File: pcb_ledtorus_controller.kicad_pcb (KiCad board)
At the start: 2 copper layers, 81 parts, among them J1 CONN_01X04, P1 CONN_4X2, P2 CONN_9, P5 CONN_3X2, P6 CONN_3, U1 TM4C1232XXPM, U3 KNUSB, U4 L6234, U5 LP2985LV, U6 TS3001x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

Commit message: Starting on netlist
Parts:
- added P3: CONN_01X09, knielsenlib:DualShock_conn, F.Cu at (76.0, 147.0)
- added P4: CONN_01X09, knielsenlib:DualShock_conn, F.Cu at (124.0, 147.0)
- added SW1: Switch_3, knielsenlib:DIPSWITCH_X3, F.Cu at (68.0, 69.0)
- J1: footprint Pin_Headers:Pin_Header_Straight_1x04_Pitch1.27mm -> Pin_Headers:Pin_Header_Straight_1x04_Pitch2.54mm
- P1: footprint Pin_Headers:Pin_Header_Straight_2x04_Pitch1.27mm -> Pin_Headers:Pin_Header_Straight_2x04_Pitch2.54mm
- P2: footprint Pin_Headers:Pin_Header_Straight_1x09_Pitch1.27mm -> Pin_Headers:Pin_Header_Straight_1x09_Pitch2.54mm
- P5: footprint Pin_Headers:Pin_Header_Straight_2x03_Pitch1.27mm -> Pin_Headers:Pin_Header_Straight_2x03_Pitch2.54mm
- moved C11 173.0 mm to (89.6, 109.4)
- moved C13 173.0 mm to (99.6, 95.1)
- moved C2 173.0 mm to (93.7, 89.8)
- moved C5 173.0 mm to (94.0, 110.5)
- moved C6 173.0 mm to (89.6, 114.4)
- moved C8 173.0 mm to (99.6, 89.8)
- moved P1 173.0 mm to (92.8, 95.0)
- moved B1 173.0 mm to (75.8, 94.8)
- moved C1 173.0 mm to (92.7, 104.1)
- moved C10 173.0 mm to (96.9, 105.4)
- moved C12 173.0 mm to (88.8, 104.1)
- moved C3 173.0 mm to (99.8, 100.4)
- moved C4 173.0 mm to (101.2, 105.4)
- moved C7 173.0 mm to (85.5, 109.4)
- moved C9 173.0 mm to (81.6, 111.6)
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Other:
- board outline added: 100 x 100 mm

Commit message: Work on layout
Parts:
- removed D8, D9: LED, LEDs:LED_0805
- removed R28, R29: 1k, Resistors_SMD:R_0805
- added H1: mounting_hole, Mounting_Holes:MountingHole_4.3mm_M4, F.Cu at (55.0, 87.0)
- added H2: mounting_hole, Mounting_Holes:MountingHole_4.3mm_M4, F.Cu at (145.0, 87.0)
- added H3: mounting_hole, Mounting_Holes:MountingHole_4.3mm_M4, F.Cu at (55.0, 142.0)
- added H4: mounting_hole, Mounting_Holes:MountingHole_4.3mm_M4, F.Cu at (145.0, 142.0)
- C15: footprint Capacitors_SMD:C_0603 -> w_smd_cap:c_elec_6.3x5.3
- D3, D5, D6, D7: footprint Diodes_SMD:D_SOD-123F -> Diodes_SMD:D_SOD-123
- P6: footprint knielsenlib:con-jack-DCJ0303 -> w_conn_misc:dc_socket
- R12, R13, R14: footprint Resistors_SMD:R_0612 -> Resistors_SMD:R_0603
- moved U3 98.0 mm to (51.5, 132.0)
- moved R22 72.6 mm to (99.9, 113.3)
- moved R30 65.7 mm to (119.7, 143.5), turned to 270 degrees
- moved R13 64.6 mm to (103.3, 118.3)
- moved R18 64.1 mm to (103.3, 120.8)
- moved R21 64.0 mm to (103.2, 113.3)
- moved R6 63.8 mm to (110.8, 115.8)
- moved D3 63.1 mm to (107.0, 115.8), turned to 180 degrees
- moved C15 60.2 mm to (107.0, 106.0), turned to 315 degrees
- moved R8 60.0 mm to (99.9, 115.8), turned to 180 degrees
- moved D5 54.7 mm to (107.0, 118.3), turned to 180 degrees
- moved SW1 54.3 mm to (56.0, 122.0), turned to 270 degrees
- moved D1 53.9 mm to (106.0, 135.5), turned to 90 degrees
- moved R19 53.9 mm to (99.9, 120.8)
- moved R14 53.8 mm to (99.9, 118.3)
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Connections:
- net Net-(C19-Pad2) renamed /Power/vsw
- net Net-(R31-Pad2) renamed /Power/fb
- P5 pad 1: +24V -> usb5v
- P5 pad 3: +8V -> +24V
- P5 pad 5: usb5v -> +8V
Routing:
- net /Motor/phase_c: track 0.00 -> 57.5 mm, vias 0 -> 4
- net /Motor/phase_a: track 0.00 -> 46.4 mm, vias 0 -> 4
- net /Motor/phase_b: track 0.00 -> 44.7 mm, vias 0 -> 4
- net +24V: track 0.00 -> 34.8 mm, vias 0 -> 3
- net /Motor/neutral: track 0.00 -> 32.3 mm, vias 0 -> 1
- net +8V: track 0.00 -> 29.5 mm
- net GND: track 0.00 -> 19.1 mm, vias 0 -> 12
- net VCC: track 0.00 -> 11.6 mm
- net /Power/vsw: track 0.00 -> 11.1 mm
- net /Power/fb: track 0.00 -> 6.75 mm
- net Net-(C19-Pad1): track 0.00 -> 3.71 mm
- net /Motor/m_sense1_raw: track 0.00 -> 2.70 mm
- net +3V3: track 0.00 -> 2.63 mm
- net /Power/bypass: track 0.00 -> 2.42 mm
- added copper zone on F.Cu, net +24V
- added copper zone on F.Cu, net +8V
- added copper zone on F.Cu, net GND
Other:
- board size 100 x 100 mm -> 100 x 68 mm
- copper layers 2 -> 4
- net class Default: clearance 0.2 -> 0; trace_width 0.25 -> 0.2032; via_dia 0.8 -> 0.635; via_drill 0.4 -> 0.3
- net class Tight added: clearance 0.1524, trace_width 0.1524, via_dia 0.635, via_drill 0.3
- rule trace_clearance: 0.2 -> 0
- rule trace_min: 0.2 -> 0.1524
- rule via_min_size: 0.4 -> 0.635

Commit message: Initial routing complete
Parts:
- moved R25 40.0 mm to (64.1, 142.9), turned to 270 degrees
- moved D2 28.8 mm to (100.3, 143.0)
- moved R5 28.8 mm to (100.3, 145.5)
- moved R22 5.73 mm to (100.5, 119.0), turned to 90 degrees
- moved D7 5.00 mm to (107.0, 118.3)
- moved R20 5.00 mm to (110.8, 118.3)
- moved R21 5.00 mm to (103.2, 118.3)
- moved R19 4.74 mm to (104.1, 123.0), turned to 180 degrees
- moved B1 3.90 mm to (66.5, 129.6)
- moved R27 3.71 mm to (95.9, 145.6), turned to 180 degrees
- moved R26 3.30 mm to (73.9, 144.7), turned to 0 degrees
- moved D3 2.50 mm to (107.0, 113.3)
- moved D5 2.50 mm to (107.0, 115.8)
- moved R12 2.50 mm to (110.8, 115.8)
- moved R13 2.50 mm to (103.3, 115.8)
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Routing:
- net usb5v: track 0.00 -> 111.7 mm, vias 0 -> 1
- net ps2_clk: track 0.00 -> 92.5 mm, vias 0 -> 1
- net m_en2: track 0.00 -> 90.8 mm, vias 0 -> 2
- net ps2_ack: track 0.00 -> 89.1 mm, vias 0 -> 1
- net ps2_data: track 0.00 -> 80.4 mm, vias 0 -> 1
- net /reset: track 0.00 -> 78.8 mm, vias 0 -> 2
- net ps2_cmd: track 0.00 -> 75.1 mm, vias 0 -> 1
- net m_en1: track 0.00 -> 74.6 mm, vias 0 -> 2
- net m_in2: track 0.00 -> 73.4 mm, vias 0 -> 2
- net m_in1: track 0.00 -> 72.1 mm, vias 0 -> 2
- net +8V: track 29.5 -> 94.3 mm
- net m_sense1: track 0.00 -> 64.1 mm, vias 0 -> 2
- net /u0rx: track 0.00 -> 54.5 mm
- net /tdi: track 0.00 -> 54.2 mm, vias 0 -> 2
- net /u0tx: track 0.00 -> 52.9 mm
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- added copper zone on In2.Cu, net +24V
- added copper zone on In2.Cu, net +3V3
- added copper zone on B.Cu, net GND
- added copper zone on In1.Cu, net GND
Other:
- net class Default: clearance 0 -> 0.2
- rule trace_clearance: 0 -> 0.2

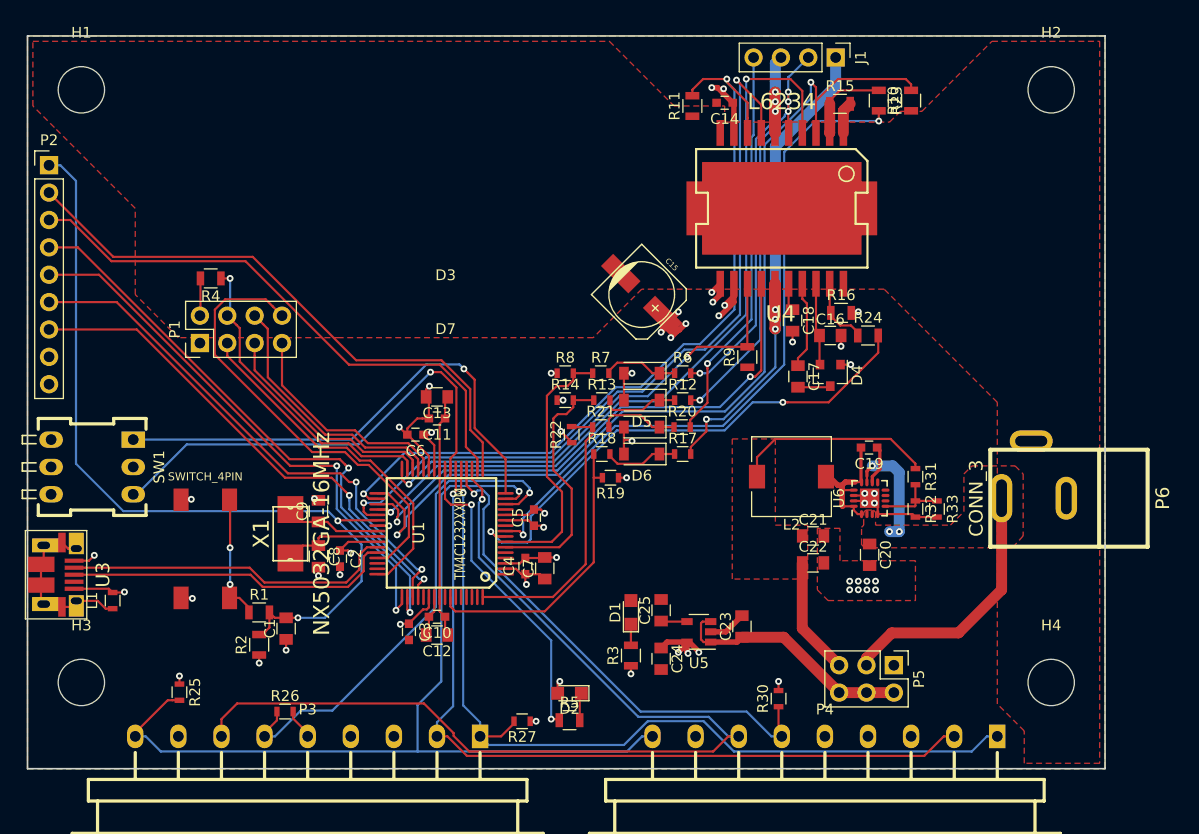
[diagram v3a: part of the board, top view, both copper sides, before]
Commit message: Completing cleanups and ToDos:
 - L6234 thermal vias done
 - Gerbers checked
 - Misc. io and stuff tweaks
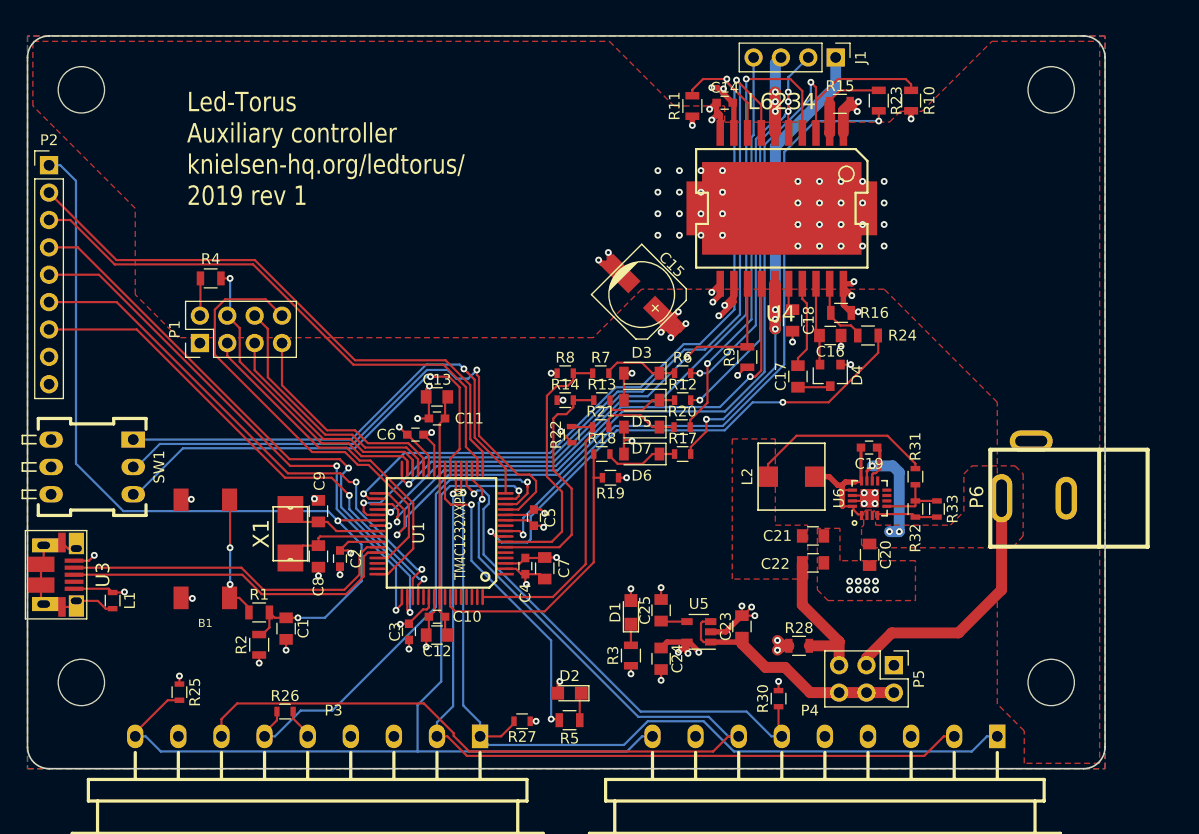
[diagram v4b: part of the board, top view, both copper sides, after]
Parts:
- added R28: 0, Resistors_SMD:R_0805, F.Cu at (121.6, 138.6)
- L2: footprint Inductors_SMD:L_7.3x7.3_H3.5 -> knielsenlib:Coil_WE_7447786004
- P6: footprint w_conn_misc:dc_socket -> knielsenlib:dc_socket
- U4: footprint knielsenlib:POWERSO20 -> knielsenlib:POWERSO20_stencil
- U6: footprint Housings_DFN_QFN:QFN-16-1EP_3x3mm_Pitch0.5mm -> knielsenlib:QFN16-TS30001
- turned L2 to 270 degrees
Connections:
- P3 pad 3: +8V -> /PS2_Controllers/rumble
- P4 pad 3: +8V -> /PS2_Controllers/rumble
- SW1 pad 1: gpio2 -> gpio3
- SW1 pad 3: Net-(SW1-Pad3) -> gpio2
- U1 pad 13: Net-(U1-Pad13) -> gpio2
- U1 pad 16: gpio2 -> gpio3
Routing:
- net /PS2_Controllers/rumble: track 0.00 -> 70.6 mm, vias 0 -> 2
- net +8V: track 94.3 -> 31.3 mm
- net gpio3: track 0.00 -> 46.9 mm, vias 0 -> 1
- net GND: track 71.0 -> 96.4 mm, vias 36 -> 92
- net gpio2: track 46.9 -> 54.0 mm
- net /Power/vsw: track 12.3 -> 13.3 mm
- net /usb_dm: track 30.9 -> 31.7 mm
- net /usb_dp: track 30.7 -> 31.6 mm
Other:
- outline, holes or cut-outs redrawn
- net class Default: clearance 0.2 -> 0
- rule trace_clearance: 0.2 -> 0
- board text added: "Led-Torus Auxiliary controller knielsen-hq.org/ledtorus/ 2019 rev 1"

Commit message: Submitted rev1 for production @ SeeedStudio
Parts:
- C15: footprint w_smd_cap:c_elec_6.3x5.3 -> w_smd_cap:c_elec_6.3x7.7
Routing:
- net +24V: track 56.9 -> 60.3 mm
- net +8V: track 31.3 -> 32.2 mm
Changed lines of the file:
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@@
     (thickness 1.6)
     (drawings 13)
-    (tracks 1038)
+    (tracks 1040)
     (zones 0)
     (modules 85)
@@
   )
   (setup
-    (last_trace_width 0.2032)
+    (last_trace_width 0.508)
     (user_trace_width 0.1524)
     (user_trace_width 0.2032)
@@
       (drillshape 0)
       (scaleselection 1)
-      (outputdirectory gerbers))
+      (outputdirectory gerbers_rev1))
   )
   (net 0 "")
@@
     (uvia_drill 0.1)
   )
+  (module w_smd_cap:c_elec_6.3x7.7 (layer F.Cu)
+    (at 107 106 315)
+    (descr "SMT capacitor, aluminium electrolytic, 6.3x7.7")
+    (fp_text reference C15 (at 0 -3.937 315) (layer F.SilkS)
+      (effects (font (size 0.50038 0.50038) (thickness 0.11938)))
+    )
+    (fp_text value 100u (at 0 3.81 315) (layer F.SilkS) hide
+      (effects (font (size 0.50038 0.50038) (thickness 0.11938)))
+    )
+    (fp_line (start -2.921 -0.762) (end -2.921 0.762) (layer F.SilkS) (width 0.127))
+    (fp_line (start -2.794 1.143) (end -2.794 -1.143) (layer F.SilkS) (width 0.127))
+    (fp_line (start -2.667 -1.397) (end -2.667 1.397) (layer F.SilkS) (width 0.127))
+    (fp_line (start -2.54 1.651) (end -2.54 -1.651) (layer F.SilkS) (width 0.127))
+    (fp_line (start -2.413 -1.778) (end -2.413 1.778) (layer F.SilkS) (width 0.127))
+    (fp_circle (center 0 0) (end -3.048 0) (layer F.SilkS) (width 0.127))
+    (fp_line (start -3.302 -3.302) (end -3.302 3.302) (layer F.SilkS) (width 0.127))
+    (fp_line (start -3.302 3.302) (end 2.54 3.302) (layer F.SilkS) (width 0.127))
+    (fp_line (start 2.54 3.302) (end 3.302 2.54) (layer F.SilkS) (width 0.127))
+    (fp_line (start 3.302 2.54) (end 3.302 -2.54) (layer F.SilkS) (width 0.127))
+    (fp_line (start 3.302 -2.54) (end 2.54 -3.302) (layer F.SilkS) (width 0.127))
+    (fp_line (start 2.54 -3.302) (end -3.302 -3.302) (layer F.SilkS) (width 0.127))
+    (fp_line (start 2.159 0) (end 1.397 0) (layer F.SilkS) (width 0.127))
+    (fp_line (start 1.778 -0.381) (end 1.778 0.381) (layer F.SilkS) (width 0.127))
+    (pad 1 smd rect (at 2.75082 0 315) (size 3.59918 1.6002) (layers F.Cu F.Paste F.Mask)
+      (net 8 +24V))
+    (pad 2 smd rect (at -2.75082 0 315) (size 3.59918 1.6002) (layers F.Cu F.Paste F.Mask)
+      (net 2 GND))
+    (model walter/smd_cap/c_elec_6_3x7_7.wrl
+      (at (xyz 0 0 0))
+      (scale (xyz 1 1 1))
+      (rotate (xyz 0 0 0))
+    )
+  )
   (module knielsenlib:POWERSO20_stencil (layer F.Cu)
     (at 120 98 180)
@@
     (pad 1 np_thru_hole circle (at 0 0) (size 4.3 4.3) (drill 4.3) (layers *.Cu *.Mask))
   )
-  (module w_smd_cap:c_elec_6.3x5.3 (layer F.Cu)
-    (at 107 106 315)
-    (descr "SMT capacitor, aluminium electrolytic, 6.3x5.3")
-    (fp_text reference C15 (at 0 -3.937 315) (layer F.SilkS)
-      (effects (font (size 1 1) (thickness 0.15)))
-    )
-    (fp_text value 100u (at 0 3.81 315) (layer F.SilkS) hide
-      (effects (font (size 0.50038 0.50038) (thickness 0.11938)))
-    )
-    (fp_line (start -2.921 -0.762) (end -2.921 0.762) (layer F.SilkS) (width 0.127))
-    (fp_line (start -2.794 1.143) (end -2.794 -1.143) (layer F.SilkS) (width 0.127))
-    (fp_line (start -2.667 -1.397) (end -2.667 1.397) (layer F.SilkS) (width 0.127))
-    (fp_line (start -2.54 1.651) (end -2.54 -1.651) (layer F.SilkS) (width 0.127))
-    (fp_line (start -2.413 -1.778) (end -2.413 1.778) (layer F.SilkS) (width 0.127))
-    (fp_circle (center 0 0) (end -3.048 0) (layer F.SilkS) (width 0.127))
-    (fp_line (start -3.302 -3.302) (end -3.302 3.302) (layer F.SilkS) (width 0.127))
-    (fp_line (start -3.302 3.302) (end 2.54 3.302) (layer F.SilkS) (width 0.127))
-    (fp_line (start 2.54 3.302) (end 3.302 2.54) (layer F.SilkS) (width 0.127))
-    (fp_line (start 3.302 2.54) (end 3.302 -2.54) (layer F.SilkS) (width 0.127))
-    (fp_line (start 3.302 -2.54) (end 2.54 -3.302) (layer F.SilkS) (width 0.127))
-    (fp_line (start 2.54 -3.302) (end -3.302 -3.302) (layer F.SilkS) (width 0.127))
-    (fp_line (start 2.159 0) (end 1.397 0) (layer F.SilkS) (width 0.127))
-    (fp_line (start 1.778 -0.381) (end 1.778 0.381) (layer F.SilkS) (width 0.127))
-    (pad 1 smd rect (at 2.750819 0 315) (size 3.59918 1.6002) (layers F.Cu F.Paste F.Mask)
-      (net 8 +24V))
-    (pad 2 smd rect (at -2.750819 0 315) (size 3.59918 1.6002) (layers F.Cu F.Paste F.Mask)
-      (net 2 GND))
-    (model walter/smd_cap/c_elec_6_3x5_3.wrl
-      (at (xyz 0 0 0))
-      (scale (xyz 1 1 1))
-      (rotate (xyz 0 0 0))
-    )
-  )
   (module Resistors_SMD:R_0603 (layer F.Cu)
     (at 110.8 115.8)
@@
   (segment (start 88.24854 122.1675) (end 88.24854 118.00146) (width 0.2032) (layer F.Cu) (net 7) (status 10))
   (segment (start 88.24854 118.00146) (end 88.75 117.5) (width 0.2032) (layer F.Cu) (net 7) (status 20))
+  (segment (start 114.153028 107.966891) (end 111.833109 107.966891) (width 0.508) (layer F.Cu) (net 8))
+  (segment (start 111.833109 107.966891) (end 111.1 108.7) (width 0.508) (layer F.Cu) (net 8))
   (segment (start 127.9 123.4) (end 127.9 122.4) (width 0.2032) (layer F.Cu) (net 8))
   (segment (start 127.9 122.4) (end 128.4 121.9) (width 0.305) (layer F.Cu) (net 8))
@@
   (segment (start 129.1 122.2) (end 129.1 120.45) (width 0.3048) (layer F.Cu) (net 13) (status 20))
   (segment (start 129.1 120.45) (end 128.85 120.2) (width 0.3048) (layer F.Cu) (net 13) (status 30))
-  (segment (start 118.725 122.9) (end 118.725 121.7468) (width 0.2032) (layer F.Cu) (net 14))
-  (segment (start 118.725 121.7468) (end 121.3718 119.1) (width 0.2032) (layer F.Cu) (net 14))
-  (segment (start 121.3718 119.1) (end 129.8032 119.1) (width 0.2032) (layer F.Cu) (net 14))
-  (segment (start 132.4 121.6968) (end 132.4 122.15) (width 0.2032) (layer F.Cu) (net 14))
+  (segment (start 118.725 122.9) (end 118.725 120.175) (width 0.2032) (layer F.Cu) (net 14))
+  (segment (start 118.725 120.175) (end 119.8 119.1) (width 0.2032) (layer F.Cu) (net 14))
+  (segment (start 119.8 119.1) (end 129.8032 119.1) (width 0.2032) (layer F.Cu) (net 14))
   (segment (start 129.8032 119.1) (end 132.4 121.6968) (width 0.2032) (layer F.Cu) (net 14))
+  (segment (start 132.4 121.6968) (end 132.4 122.15) (width 0.2032) (layer F.Cu) (net 14))
   (segment (start 125.32 138.22) (end 124.94 138.6) (width 1.016) (layer F.Cu) (net 14))
   (segment (start 124.94 138.6) (end 122.55 138.6) (width 1.016) (layer F.Cu) (net 14) (status 20))
